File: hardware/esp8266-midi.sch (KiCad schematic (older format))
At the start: 21 parts, among them J1 MIDI in, J2 MIDI out, J3 TTL-232R-3V3 connector, J4 Bat+, J5 Bat-, SW1 reset, SW2 Prog enable, U1 ESP-12F, U2 6N138, U3 LD1117S50TR_SOT223

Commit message: Initial rev of schematic and PCB, WIP
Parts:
- added C5: 220uF, Capacitors_THT:CP_Radial_D5.0mm_P2.50mm, symbol CP
- D1: footprint Diodes_THT:D_DO-41_SOD81_P10.16mm_Horizontal -> Diodes_THT:D_A-405_P10.16mm_Horizontal
- R1, R3, R4, R6: footprint Resistors_THT:R_Axial_DIN0204_L3.6mm_D1.6mm_P7.62mm_Horizontal -> Resistors_THT:R_Axial_DIN0207_L6.3mm_D2.5mm_P10.16mm_Horizontal
- R2, R5: value 430R -> 220R; footprint Resistors_THT:R_Axial_DIN0204_L3.6mm_D1.6mm_P7.62mm_Horizontal -> Resistors_THT:R_Axial_DIN0207_L6.3mm_D2.5mm_P10.16mm_Horizontal
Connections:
- wire segments 75 -> 78
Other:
- moved on the sheet: D1, J4, J5
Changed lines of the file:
@@
 P 7650 4100
 F 0 "R2" V 7730 4100 50  0000 C CNN
-F 1 "430R" V 7650 4100 50  0000 C CNN
-F 2 "Resistors_THT:R_Axial_DIN0204_L3.6mm_D1.6mm_P7.62mm_Horizontal" V 7580 4100 50  0001 C CNN
+F 1 "220R" V 7650 4100 50  0000 C CNN
+F 2 "Resistors_THT:R_Axial_DIN0207_L6.3mm_D2.5mm_P10.16mm_Horizontal" V 7580 4100 50  0001 C CNN
 F 3 "" H 7650 4100 50  0001 C CNN
 	1    7650 4100
@@
 P 6550 4100
 F 0 "R5" V 6630 4100 50  0000 C CNN
-F 1 "430R" V 6550 4100 50  0000 C CNN
-F 2 "Resistors_THT:R_Axial_DIN0204_L3.6mm_D1.6mm_P7.62mm_Horizontal" V 6480 4100 50  0001 C CNN
+F 1 "220R" V 6550 4100 50  0000 C CNN
+F 2 "Resistors_THT:R_Axial_DIN0207_L6.3mm_D2.5mm_P10.16mm_Horizontal" V 6480 4100 50  0001 C CNN
 F 3 "" H 6550 4100 50  0001 C CNN
 	1    6550 4100
@@
 L D D1
 U 1 1 5AA1AFB6
-P 8300 5700
-F 0 "D1" H 8300 5800 50  0000 C CNN
-F 1 "D" H 8300 5600 50  0000 C CNN
-F 2 "Diodes_THT:D_DO-41_SOD81_P10.16mm_Horizontal" H 8300 5700 50  0001 C CNN
-F 3 "" H 8300 5700 50  0001 C CNN
-	1    8300 5700
-	-1   0    0    1
+P 8050 5400
+F 0 "D1" H 8050 5500 50  0000 C CNN
+F 1 "D" H 8050 5300 50  0000 C CNN
+F 2 "Diodes_THT:D_A-405_P10.16mm_Horizontal" H 8050 5400 50  0001 C CNN
+F 3 "" H 8050 5400 50  0001 C CNN
+	1    8050 5400
+	0    -1   -1   0
 $EndComp
 $Comp
@@
 F 0 "R1" V 8780 5700 50  0000 C CNN
 F 1 "220R" V 8700 5700 50  0000 C CNN
-F 2 "Resistors_THT:R_Axial_DIN0204_L3.6mm_D1.6mm_P7.62mm_Horizontal" V 8630 5700 50  0001 C CNN
+F 2 "Resistors_THT:R_Axial_DIN0207_L6.3mm_D2.5mm_P10.16mm_Horizontal" V 8630 5700 50  0001 C CNN
 F 3 "" H 8700 5700 50  0001 C CNN
 	1    8700 5700
@@
 $EndComp
 Wire Wire Line
-	8450 5700 8550 5700
-Wire Wire Line
 	8850 5700 8950 5700
 Wire Wire Line
@@
 	8950 5100 8800 5100
 Wire Wire Line
-	8050 5700 8150 5700
-Wire Wire Line
 	8050 5100 8200 5100
-Wire Wire Line
-	8500 5700 8500 5850
-Wire Wire Line
-	8500 5850 7950 5850
-Wire Wire Line
-	7950 5850 7950 5350
-Connection ~ 8500 5700
-Wire Wire Line
-	7950 5350 7850 5350
-Wire Wire Line
-	8050 5100 8050 5700
-Wire Wire Line
-	8050 5550 7850 5550
-Connection ~ 8050 5550
 $Comp
 L R R3
@@
 F 0 "R3" V 7230 5150 50  0000 C CNN
 F 1 "470R" V 7150 5150 50  0000 C CNN
-F 2 "Resistors_THT:R_Axial_DIN0204_L3.6mm_D1.6mm_P7.62mm_Horizontal" V 7080 5150 50  0001 C CNN
+F 2 "Resistors_THT:R_Axial_DIN0207_L6.3mm_D2.5mm_P10.16mm_Horizontal" V 7080 5150 50  0001 C CNN
 F 3 "" H 7150 5150 50  0001 C CNN
 	1    7150 5150
@@
 F 0 "R4" V 7230 5400 50  0000 C CNN
 F 1 "10K" V 7150 5400 50  0000 C CNN
-F 2 "Resistors_THT:R_Axial_DIN0204_L3.6mm_D1.6mm_P7.62mm_Horizontal" V 7080 5400 50  0001 C CNN
+F 2 "Resistors_THT:R_Axial_DIN0207_L6.3mm_D2.5mm_P10.16mm_Horizontal" V 7080 5400 50  0001 C CNN
 F 3 "" H 7150 5400 50  0001 C CNN
 	1    7150 5400
@@
 F 0 "R6" V 3830 4650 50  0000 C CNN
 F 1 "1K" V 3750 4650 50  0000 C CNN
-F 2 "Resistors_THT:R_Axial_DIN0204_L3.6mm_D1.6mm_P7.62mm_Horizontal" V 3680 4650 50  0001 C CNN
+F 2 "Resistors_THT:R_Axial_DIN0207_L6.3mm_D2.5mm_P10.16mm_Horizontal" V 3680 4650 50  0001 C CNN
 F 3 "" H 3750 4650 50  0001 C CNN
 	1    3750 4650
@@
 $EndComp
 Wire Wire Line
-	4850 1850 5150 1850
-Wire Wire Line
-	5050 1950 5050 1850
-Connection ~ 5050 1850
-Wire Wire Line
 	5750 1850 6400 1850
 Wire Wire Line
@@
 Connection ~ 6200 1850
 Wire Wire Line
-	4850 2350 6200 2350
+	4500 2350 6200 2350
 Wire Wire Line
 	6200 2350 6200 2250
@@
 	5850 2250 5850 2350
 Connection ~ 5850 2350
-Wire Wire Line
-	5050 2250 5050 2350
-Connection ~ 5050 2350
 Wire Wire Line
 	5450 2150 5450 2450
@@
 L Conn_01x01_Male J4
 U 1 1 5AA3271F
-P 4650 1850
-F 0 "J4" H 4650 1950 50  0000 C CNN
-F 1 "Bat+" H 4650 1750 50  0000 C CNN
-F 2 "Wire_Pads:SolderWirePad_single_0-8mmDrill" H 4650 1850 50  0001 C CNN
-F 3 "" H 4650 1850 50  0001 C CNN
-	1    4650 1850
+P 4300 1850
+F 0 "J4" H 4300 1950 50  0000 C CNN
+F 1 "Bat+" H 4300 1750 50  0000 C CNN
+F 2 "Wire_Pads:SolderWirePad_single_0-8mmDrill" H 4300 1850 50  0001 C CNN
+F 3 "" H 4300 1850 50  0001 C CNN
+	1    4300 1850
 	1    0    0    -1
 $EndComp
@@
 L Conn_01x01_Male J5
 U 1 1 5AA327AB
-P 4650 2350
-F 0 "J5" H 4650 2450 50  0000 C CNN
-F 1 "Bat-" H 4650 2250 50  0000 C CNN
-F 2 "Wire_Pads:SolderWirePad_single_0-8mmDrill" H 4650 2350 50  0001 C CNN
-F 3 "" H 4650 2350 50  0001 C CNN
-	1    4650 2350
-	1    0    0    -1
-$EndComp
+P 4300 2350
+F 0 "J5" H 4300 2450 50  0000 C CNN
+F 1 "Bat-" H 4300 2250 50  0000 C CNN
+F 2 "Wire_Pads:SolderWirePad_single_0-8mmDrill" H 4300 2350 50  0001 C CNN
+F 3 "" H 4300 2350 50  0001 C CNN
+	1    4300 2350
+	1    0    0    -1
+$EndComp
+Wire Wire Line
+	8050 5100 8050 5250
+Wire Wire Line
+	8050 5550 8050 5700
+Wire Wire Line
+	8050 5700 8550 5700
+Wire Wire Line
+	7850 5550 7900 5550
+Wire Wire Line
+	7900 5550 7900 5200
+Wire Wire Line
+	7900 5200 8050 5200
+Connection ~ 8050 5200
+Wire Wire Line
+	7850 5350 7950 5350
+Wire Wire Line
+	7950 5350 7950 5600
+Wire Wire Line
+	7950 5600 8050 5600
+Connection ~ 8050 5600
+$Comp
+L CP C5
+U 1 1 5AA5095E
+P 4700 2100
+F 0 "C5" H 4725 2200 50  0000 L CNN
+F 1 "220uF" H 4725 2000 50  0000 L CNN
+F 2 "Capacitors_THT:CP_Radial_D5.0mm_P2.50mm" H 4738 1950 50  0001 C CNN
+F 3 "" H 4700 2100 50  0001 C CNN
+	1    4700 2100
+	1    0    0    -1
+$EndComp
+Wire Wire Line
+	4500 1850 5150 1850
+Connection ~ 5050 1850
+Wire Wire Line
+	5050 1850 5050 1950
+Wire Wire Line
+	5050 2250 5050 2350
+Connection ~ 5050 2350
+Wire Wire Line
+	4700 1950 4700 1850
+Connection ~ 4700 1850
+Wire Wire Line
+	4700 2250 4700 2350
+Connection ~ 4700 2350
 $EndSCHEMATC

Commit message: Update schematic: now uses ESP-12E footprint from standard KiCad lib
+ Misc silly fixes.
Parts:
- removed U1: ESP-12F, RF_Modules:ESP-12E, symbol ESP-12F
- added R7: 10K, Resistors_THT:R_Axial_DIN0207_L6.3mm_D2.5mm_P10.16mm_Horizontal, symbol R-RESCUE-esp8266-midi
- added U1: ESP-12E, RF_Modules:ESP-12E, symbol ESP-12E
- C2, C3: symbol C -> C-RESCUE-esp8266-midi
- D1: value D -> 1N4148
- R1, R2, R3, R4, R5, R6: symbol R -> R-RESCUE-esp8266-midi
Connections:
- wire segments 78 -> 76
- no-connect marks 18 -> 19
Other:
- note added: "Try R4 with 1K or\n2.7K as well."
- moved on the sheet: C1, D1, J1, J2, J3, R1, R2, R3, R4, R5, R6, U2

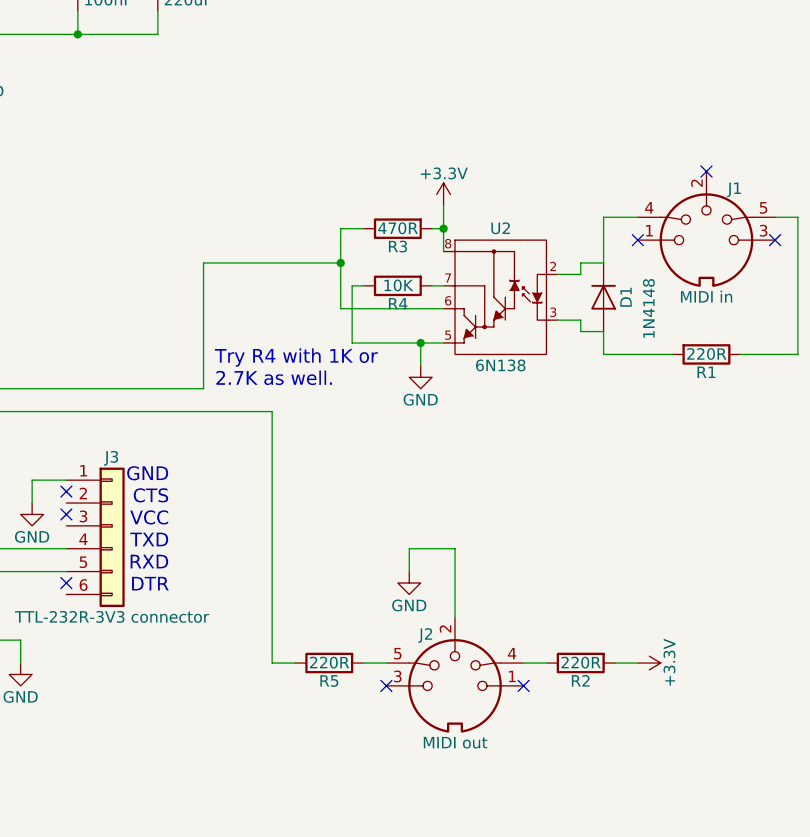
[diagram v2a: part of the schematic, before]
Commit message: Schematic change: do not pull up opto-isolator output + change output resistor loop values
1. Pull up can be done by the micro itself.
2. 220 ohm examples are taken from Midi spec when voltage is 5v. To match the
   the same current when using 3.3v micro resistors were reduced to 120ohm.
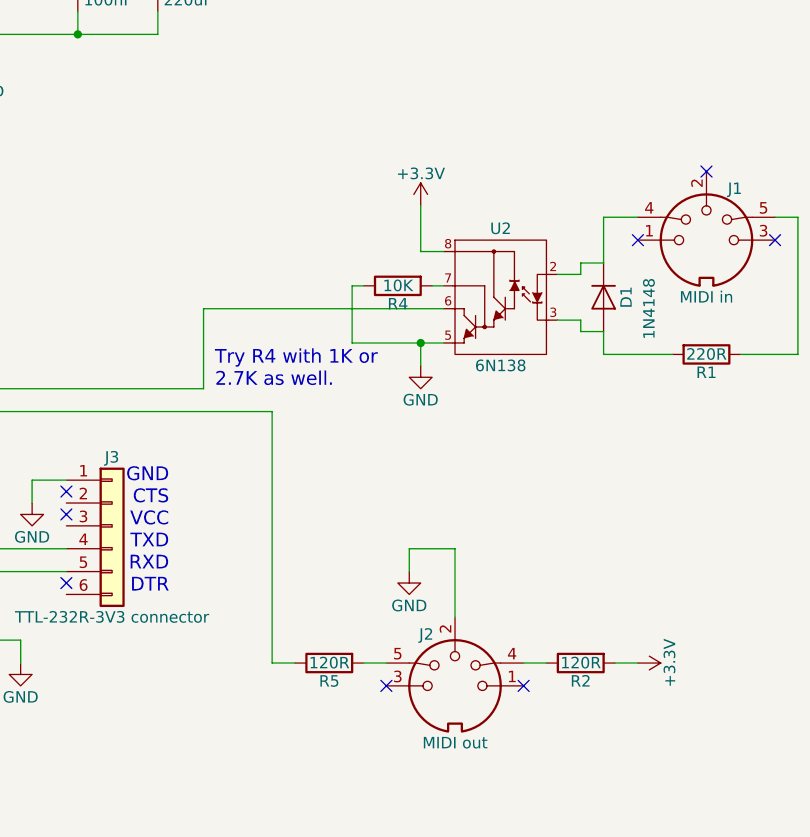
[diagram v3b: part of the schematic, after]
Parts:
- removed R3: 470R, Resistors_THT:R_Axial_DIN0207_L6.3mm_D2.5mm_P10.16mm_Horizontal, symbol R-RESCUE-esp8266-midi
- R2, R5: value 220R -> 120R
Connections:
- wire segments 76 -> 73
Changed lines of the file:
@@
 P 8050 5100
 F 0 "R2" V 8130 5100 50  0000 C CNN
-F 1 "220R" V 8050 5100 50  0000 C CNN
+F 1 "120R" V 8050 5100 50  0000 C CNN
 F 2 "Resistors_THT:R_Axial_DIN0207_L6.3mm_D2.5mm_P10.16mm_Horizontal" V 7980 5100 50  0001 C CNN
 F 3 "" H 8050 5100 50  0001 C CNN
@@
 P 6950 5100
 F 0 "R5" V 7030 5100 50  0000 C CNN
-F 1 "220R" V 6950 5100 50  0000 C CNN
+F 1 "120R" V 6950 5100 50  0000 C CNN
 F 2 "Resistors_THT:R_Axial_DIN0207_L6.3mm_D2.5mm_P10.16mm_Horizontal" V 6880 5100 50  0001 C CNN
 F 3 "" H 6950 5100 50  0001 C CNN
@@
 $EndComp
 $Comp
-L R-RESCUE-esp8266-midi R3
-U 1 1 5AA1C317
-P 7250 3200
-F 0 "R3" V 7330 3200 50  0000 C CNN
-F 1 "470R" V 7250 3200 50  0000 C CNN
-F 2 "Resistors_THT:R_Axial_DIN0207_L6.3mm_D2.5mm_P10.16mm_Horizontal" V 7180 3200 50  0001 C CNN
-F 3 "" H 7250 3200 50  0001 C CNN
-	1    7250 3200
-	0    -1   1    0
-$EndComp
-$Comp
 L R-RESCUE-esp8266-midi R4
 U 1 1 5AA1C352
@@
 $EndComp
 Wire Wire Line
-	7450 3100 7450 3300
-Wire Wire Line
-	7450 3200 7400 3200
-Wire Wire Line
 	7450 3450 7400 3450
 Wire Wire Line
@@
 L +3.3V #PWR03
 U 1 1 5AA1C85B
-P 7450 3100
-F 0 "#PWR03" H 7450 2950 50  0001 C CNN
-F 1 "+3.3V" H 7450 3240 50  0000 C CNN
-F 2 "" H 7450 3100 50  0001 C CNN
-F 3 "" H 7450 3100 50  0001 C CNN
-	1    7450 3100
+P 7350 3100
+F 0 "#PWR03" H 7350 2950 50  0001 C CNN
+F 1 "+3.3V" H 7350 3240 50  0000 C CNN
+F 2 "" H 7350 3100 50  0001 C CNN
+F 3 "" H 7350 3100 50  0001 C CNN
+	1    7350 3100
 	-1   0    0    -1
 $EndComp
-Connection ~ 7450 3200
 $Comp
 L GND #PWR04
@@
 	2600 3800 2600 3900
 Wire Wire Line
-	7000 3200 7000 3550
-Wire Wire Line
-	7000 3550 7450 3550
+	6400 3550 7450 3550
 NoConn ~ 7200 5200
 NoConn ~ 7800 5200
@@
 	5100 3900 6400 3900
 Wire Wire Line
-	6400 3900 6400 3350
-Wire Wire Line
-	6400 3350 7000 3350
-Connection ~ 7000 3350
-Wire Wire Line
-	7000 3200 7100 3200
+	6400 3900 6400 3550
 NoConn ~ 5800 4750
 NoConn ~ 5800 4450
@@
 Wire Wire Line
 	5500 4600 5800 4600
+Wire Wire Line
+	7350 3100 7350 3300
+Wire Wire Line
+	7350 3300 7450 3300
 $EndSCHEMATC

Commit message: Before resizing the board a bit
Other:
- note added: "TODO: solder GPIO16 back and test it"
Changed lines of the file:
@@
 Wire Wire Line
 	7350 3300 7450 3300
+Text Notes 4950 3050 0    60   ~ 0
+TODO: solder GPIO16 back and test it
 $EndSCHEMATC

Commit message: Misc cleanup: remove some TODOs/notes. Schematic is verified / works.
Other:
- note removed: "TODO: solder GPIO16 back and test it"
- note removed: "Try R4 with 1K or\n2.7K as well."
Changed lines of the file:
@@
 Wire Wire Line
 	8150 3150 8300 3150
-Text Notes 6450 3900 0    60   ~ 0
-Try R4 with 1K or\n2.7K as well.
 $Comp
 L ESP-12E U1
@@
 Wire Wire Line
 	7350 3300 7450 3300
-Text Notes 4950 3050 0    60   ~ 0
-TODO: solder GPIO16 back and test it
 $EndSCHEMATC

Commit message: Change schematic to use external flash enable + reset circuit
Less components + all those switches are expensive and cumbersome to use ;)

And another misc change: remove a probs redundant power supply smoothing
capacitor.
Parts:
- removed C1: 1uF, Capacitors_THT:CP_Radial_D4.0mm_P2.00mm, symbol CP
- removed C5: 220uF, Capacitors_THT:CP_Radial_D5.0mm_P2.50mm, symbol CP
- removed R6: 1K, Resistors_THT:R_Axial_DIN0207_L6.3mm_D2.5mm_P10.16mm_Horizontal, symbol R-RESCUE-esp8266-midi
- removed SW1: reset, Buttons_Switches_THT:SW_PUSH_6mm, symbol SW_Push
- removed SW2: Prog enable, Buttons_Switches_THT:SW_PUSH_6mm, symbol SW_Push
- added R? (x3): 10K, symbol R
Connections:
- wire segments 73 -> 69
- no-connect marks 19 -> 18
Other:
- note added: "GND\nFLASH\nVCC\nTXD\nRXD\nRESET"
- note removed: "GND\nCTS\nVCC\nTXD\nRXD\nDTR"
- moved on the sheet: J4, J5

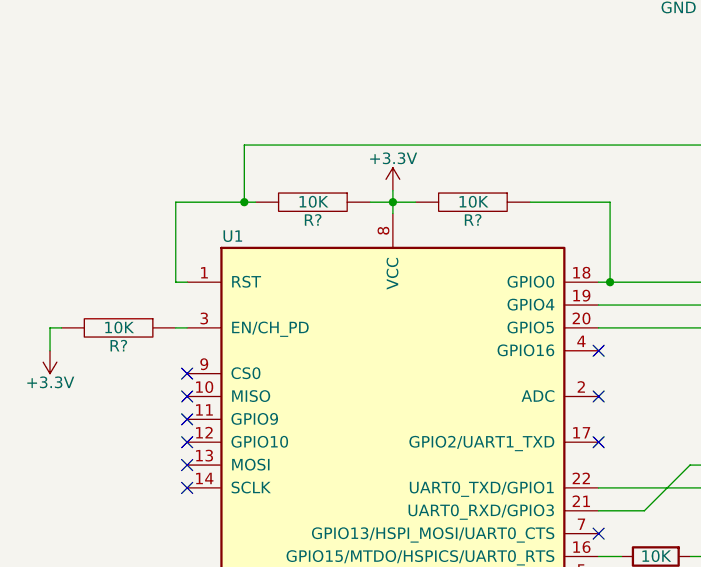
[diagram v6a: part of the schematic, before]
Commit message: Assign SMD footprints to (almost) all components
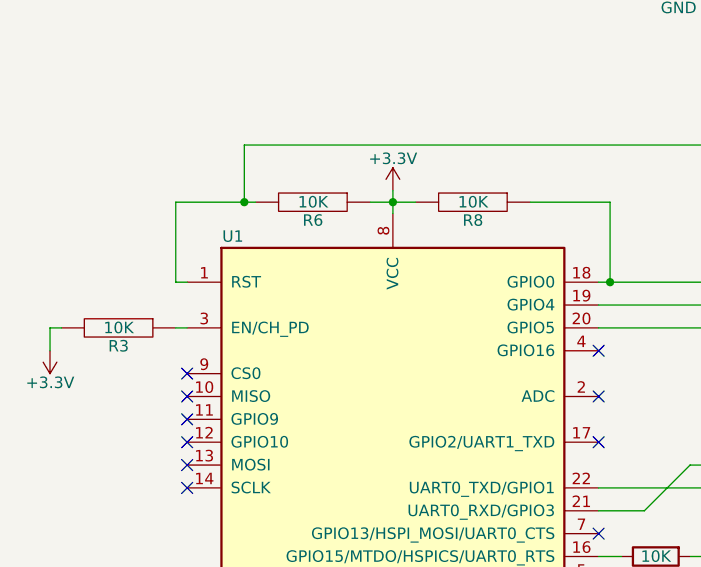
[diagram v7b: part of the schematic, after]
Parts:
- C2, C3: footprint Capacitors_THT:C_Disc_D3.8mm_W2.6mm_P2.50mm -> Capacitors_SMD:C_0805_HandSoldering
- C4: footprint Capacitors_THT:CP_Radial_D5.0mm_P2.50mm -> Capacitors_SMD:CP_Elec_6.3x5.8
- D1: footprint Diodes_THT:D_A-405_P10.16mm_Horizontal -> Diodes_SMD:D_SOD-323_HandSoldering
- R1, R2, R4, R5, R7: footprint Resistors_THT:R_Axial_DIN0207_L6.3mm_D2.5mm_P10.16mm_Horizontal -> Resistors_SMD:R_0805_HandSoldering
- R3, R6, R8: renamed from R?; footprint (none) -> Resistors_SMD:R_0805_HandSoldering
- U2: footprint Housings_DIP:DIP-8_W7.62mm -> Housings_DIP:DIP-8_W7.62mm_SMDSocket_SmallPads
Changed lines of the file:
@@
 F 0 "R2" V 8130 5100 50  0000 C CNN
 F 1 "120R" V 8050 5100 50  0000 C CNN
-F 2 "Resistors_THT:R_Axial_DIN0207_L6.3mm_D2.5mm_P10.16mm_Horizontal" V 7980 5100 50  0001 C CNN
+F 2 "Resistors_SMD:R_0805_HandSoldering" V 7980 5100 50  0001 C CNN
 F 3 "" H 8050 5100 50  0001 C CNN
 	1    8050 5100
@@
 F 0 "R5" V 7030 5100 50  0000 C CNN
 F 1 "120R" V 6950 5100 50  0000 C CNN
-F 2 "Resistors_THT:R_Axial_DIN0207_L6.3mm_D2.5mm_P10.16mm_Horizontal" V 6880 5100 50  0001 C CNN
+F 2 "Resistors_SMD:R_0805_HandSoldering" V 6880 5100 50  0001 C CNN
 F 3 "" H 6950 5100 50  0001 C CNN
 	1    6950 5100
@@
 F 0 "U2" H 7700 3800 50  0000 C CNN
 F 1 "6N138" H 7700 3200 50  0000 C CNN
-F 2 "Housings_DIP:DIP-8_W7.62mm" H 7700 3500 60  0001 C CNN
+F 2 "Housings_DIP:DIP-8_W7.62mm_SMDSocket_SmallPads" H 7700 3500 60  0001 C CNN
 F 3 "" H 7700 3500 60  0000 C CNN
 	1    7700 3500
@@
 F 0 "D1" H 8150 3600 50  0000 C CNN
 F 1 "1N4148" H 8200 3700 50  0000 C CNN
-F 2 "Diodes_THT:D_A-405_P10.16mm_Horizontal" H 8150 3500 50  0001 C CNN
+F 2 "Diodes_SMD:D_SOD-323_HandSoldering" H 8150 3500 50  0001 C CNN
 F 3 "" H 8150 3500 50  0001 C CNN
 	1    8150 3500
@@
 F 0 "R1" V 8680 3750 50  0000 C CNN
 F 1 "220R" V 8600 3750 50  0000 C CNN
-F 2 "Resistors_THT:R_Axial_DIN0207_L6.3mm_D2.5mm_P10.16mm_Horizontal" V 8530 3750 50  0001 C CNN
+F 2 "Resistors_SMD:R_0805_HandSoldering" V 8530 3750 50  0001 C CNN
 F 3 "" H 8600 3750 50  0001 C CNN
 	1    8600 3750
@@
 F 0 "R4" V 7330 3450 50  0000 C CNN
 F 1 "10K" V 7250 3450 50  0000 C CNN
-F 2 "Resistors_THT:R_Axial_DIN0207_L6.3mm_D2.5mm_P10.16mm_Horizontal" V 7180 3450 50  0001 C CNN
+F 2 "Resistors_SMD:R_0805_HandSoldering" V 7180 3450 50  0001 C CNN
 F 3 "" H 7250 3450 50  0001 C CNN
 	1    7250 3450
@@
 F 0 "C4" H 6225 2200 50  0000 L CNN
 F 1 "220uF" H 6225 2000 50  0000 L CNN
-F 2 "Capacitors_THT:CP_Radial_D5.0mm_P2.50mm" H 6238 1950 50  0001 C CNN
+F 2 "Capacitors_SMD:CP_Elec_6.3x5.8" H 6238 1950 50  0001 C CNN
 F 3 "" H 6200 2100 50  0001 C CNN
 	1    6200 2100
@@
 F 0 "C3" H 5875 2200 50  0000 L CNN
 F 1 "100nF" H 5875 2000 50  0000 L CNN
-F 2 "Capacitors_THT:C_Disc_D3.8mm_W2.6mm_P2.50mm" H 5888 1950 50  0001 C CNN
+F 2 "Capacitors_SMD:C_0805_HandSoldering" H 5888 1950 50  0001 C CNN
 F 3 "" H 5850 2100 50  0001 C CNN
 	1    5850 2100
@@
 F 0 "C2" H 5075 2200 50  0000 L CNN
 F 1 "100nF" H 5075 2000 50  0000 L CNN
-F 2 "Capacitors_THT:C_Disc_D3.8mm_W2.6mm_P2.50mm" H 5088 1950 50  0001 C CNN
+F 2 "Capacitors_SMD:C_0805_HandSoldering" H 5088 1950 50  0001 C CNN
 F 3 "" H 5050 2100 50  0001 C CNN
 	1    5050 2100
@@
 $EndComp
 $Comp
-L +3.3V #PWR08
+L +3.3V #PWR06
 U 1 1 5AA308D3
 P 6400 1850
-F 0 "#PWR08" H 6400 1700 50  0001 C CNN
+F 0 "#PWR06" H 6400 1700 50  0001 C CNN
 F 1 "+3.3V" H 6400 1990 50  0000 C CNN
 F 2 "" H 6400 1850 50  0001 C CNN
@@
 $EndComp
 $Comp
-L GND #PWR09
+L GND #PWR07
 U 1 1 5AA310B5
 P 5450 2450
-F 0 "#PWR09" H 5450 2200 50  0001 C CNN
+F 0 "#PWR07" H 5450 2200 50  0001 C CNN
 F 1 "GND" H 5450 2300 50  0000 C CNN
 F 2 "" H 5450 2450 50  0001 C CNN
@@
 F 0 "R7" V 5430 5000 50  0000 C CNN
 F 1 "10K" V 5350 5000 50  0000 C CNN
-F 2 "Resistors_THT:R_Axial_DIN0207_L6.3mm_D2.5mm_P10.16mm_Horizontal" V 5280 5000 50  0001 C CNN
+F 2 "Resistors_SMD:R_0805_HandSoldering" V 5280 5000 50  0001 C CNN
 F 3 "" H 5350 5000 50  0001 C CNN
 	1    5350 5000
@@
 $EndComp
 $Comp
-L GND #PWR010
+L GND #PWR08
 U 1 1 5AC3E798
 P 4200 5800
-F 0 "#PWR010" H 4200 5550 50  0001 C CNN
+F 0 "#PWR08" H 4200 5550 50  0001 C CNN
 F 1 "GND" H 4200 5650 50  0000 C CNN
 F 2 "" H 4200 5800 50  0001 C CNN
@@
 $EndComp
 $Comp
-L +3.3V #PWR011
+L +3.3V #PWR09
 U 1 1 5AC3F393
 P 4200 3400
-F 0 "#PWR011" H 4200 3250 50  0001 C CNN
+F 0 "#PWR09" H 4200 3250 50  0001 C CNN
 F 1 "+3.3V" H 4200 3540 50  0000 C CNN
 F 2 "" H 4200 3400 50  0001 C CNN
@@
 $EndComp
 $Comp
-L +3.3V #PWR012
+L +3.3V #PWR010
 U 1 1 5AC3FC81
 P 2700 4100
-F 0 "#PWR012" H 2700 3950 50  0001 C CNN
+F 0 "#PWR010" H 2700 3950 50  0001 C CNN
 F 1 "+3.3V" H 2700 4240 50  0000 C CNN
 F 2 "" H 2700 4100 50  0001 C CNN
@@
 $EndComp
 $Comp
-L GND #PWR013
+L GND #PWR011
 U 1 1 5AC41342
 P 5600 5100
-F 0 "#PWR013" H 5600 4850 50  0001 C CNN
+F 0 "#PWR011" H 5600 4850 50  0001 C CNN
 F 1 "GND" H 5600 4950 50  0000 C CNN
 F 2 "" H 5600 5100 50  0001 C CNN
@@
 NoConn ~ 5100 4300
 $Comp
-L R R?
+L R R6
 U 1 1 5B127227
 P 3850 3450
-F 0 "R?" V 3930 3450 50  0000 C CNN
+F 0 "R6" V 3930 3450 50  0000 C CNN
 F 1 "10K" V 3850 3450 50  0000 C CNN
-F 2 "" H 3850 3450 50  0001 C CNN
+F 2 "Resistors_SMD:R_0805_HandSoldering" H 3850 3450 50  0001 C CNN
 F 3 "" H 3850 3450 50  0001 C CNN
 	1    3850 3450
@@
 $EndComp
 $Comp
-L R R?
+L R R8
 U 1 1 5B1275B7
 P 4550 3450
-F 0 "R?" V 4630 3450 50  0000 C CNN
+F 0 "R8" V 4630 3450 50  0000 C CNN
 F 1 "10K" V 4550 3450 50  0000 C CNN
-F 2 "" H 4550 3450 50  0001 C CNN
+F 2 "Resistors_SMD:R_0805_HandSoldering" H 4550 3450 50  0001 C CNN
 F 3 "" H 4550 3450 50  0001 C CNN
 	1    4550 3450
@@
 	3250 3800 3300 3800
 $Comp
-L R R?
+L R R3
 U 1 1 5B12802D
 P 3000 4000
-F 0 "R?" V 3080 4000 50  0000 C CNN
+F 0 "R3" V 3080 4000 50  0000 C CNN
 F 1 "10K" V 3000 4000 50  0000 C CNN
-F 2 "" H 3000 4000 50  0001 C CNN
+F 2 "Resistors_SMD:R_0805_HandSoldering" H 3000 4000 50  0001 C CNN
 F 3 "" H 3000 4000 50  0001 C CNN
 	1    3000 4000
